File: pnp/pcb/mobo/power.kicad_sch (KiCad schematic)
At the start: 30 parts, among them J31 Barrel_Jack_Switch, J34 Screw_Terminal_01x02, U11 FDS4435BZ, U12 TPS54331, U13 AP1117-33

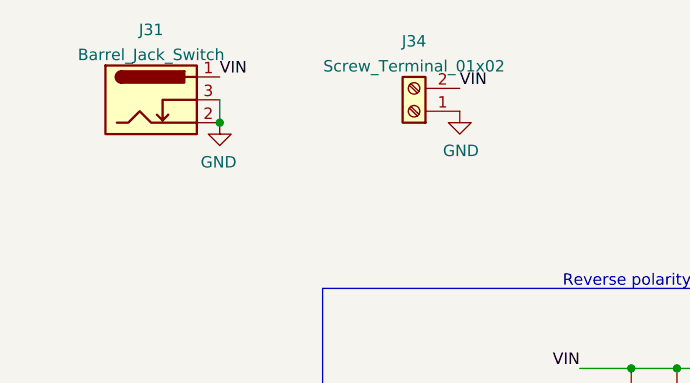
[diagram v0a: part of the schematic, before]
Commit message: adds custom combo power jack footprint for both barrel jack and terminal block
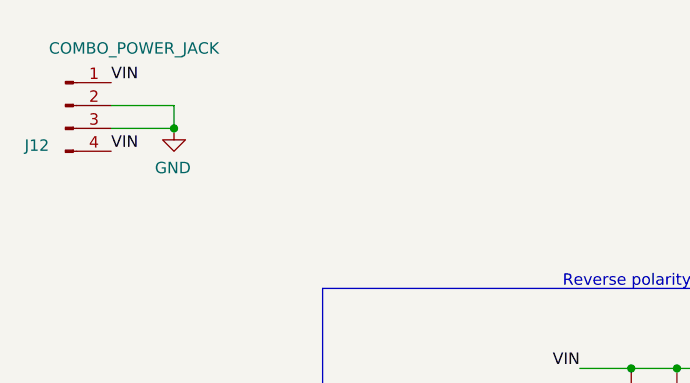
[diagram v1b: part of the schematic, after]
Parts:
- removed J31: Barrel_Jack_Switch, Connector_BarrelJack:BarrelJack_Horizontal, symbol Connector:Barrel_Jack_Switch
- removed J34: Screw_Terminal_01x02, TerminalBlock_RND:TerminalBlock_RND_205-00001_1x02_P5.00mm_Horizontal, symbol Connector:Screw_Terminal_01x02
- added J12: COMBO_POWER_JACK, index:BarrelJack_Horizontal, symbol Connector:Conn_01x04_Male
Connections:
- net GND: now also J12.2 (Pin_2), J12.3 (Pin_3)
- net VIN: now also J12.1 (Pin_1), J12.4 (Pin_4)
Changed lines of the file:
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@@
   (junction (at 121.92 55.88) (diameter 0) (color 0 0 0 0)
   )
+  (junction (at 45.72 29.21) (diameter 0) (color 0 0 0 0)
+  )
   (junction (at 121.92 64.77) (diameter 0) (color 0 0 0 0)
   )
@@
   )
   (junction (at 118.11 104.14) (diameter 0) (color 0 0 0 0)
-  )
-  (junction (at 50.8 28.575) (diameter 0) (color 0 0 0 0)
   )
   (junction (at 158.75 140.97) (diameter 0) (color 0 0 0 0)
@@
     (stroke (width 0) (type default) (color 0 0 0 0))
   )
+  (wire (pts (xy 38.735 29.21) (xy 45.72 29.21))
+    (stroke (width 0) (type default) (color 0 0 0 0))
+  )
   (polyline (pts (xy 167.64 157.48) (xy 134.62 157.48))
     (stroke (width 0) (type default) (color 0 0 0 0))
@@
     (stroke (width 0) (type default) (color 0 0 0 0))
   )
+  (wire (pts (xy 38.735 26.67) (xy 45.72 26.67))
+    (stroke (width 0) (type default) (color 0 0 0 0))
+  )
   (wire (pts (xy 182.88 100.33) (xy 182.88 101.6))
     (stroke (width 0) (type default) (color 0 0 0 0))
@@
     (stroke (width 0) (type default) (color 0 0 0 0))
   )
+  (wire (pts (xy 45.72 26.67) (xy 45.72 29.21))
+    (stroke (width 0) (type default) (color 0 0 0 0))
+  )
   (wire (pts (xy 121.92 64.77) (xy 123.19 64.77))
     (stroke (width 0) (type default) (color 0 0 0 0))
@@
   )
   (wire (pts (xy 92.71 152.4) (xy 97.79 152.4))
-    (stroke (width 0) (type default) (color 0 0 0 0))
-  )
-  (wire (pts (xy 50.8 26.035) (xy 50.8 28.575))
     (stroke (width 0) (type default) (color 0 0 0 0))
   )
@@
     (effects (font (size 1.27 1.27)) (justify right bottom))
   )
-  (label "VIN" (at 77.47 24.765 0)
+  (label "VIN" (at 38.735 31.75 0)
     (effects (font (size 1.27 1.27)) (justify left bottom))
   )
-  (label "VIN" (at 50.8 23.495 0)
+  (label "VIN" (at 38.735 24.13 0)
     (effects (font (size 1.27 1.27)) (justify left bottom))
   )
@@
     (pin "1")
   )
-  (symbol (lib_id "Connector:Screw_Terminal_01x02") (at 72.39 27.305 180) (unit 1)
-    (in_bom yes) (on_board yes) (fields_autoplaced)
-    (property "Reference" "J34" (id 0) (at 72.39 19.5285 0))
-    (property "Value" "Screw_Terminal_01x02" (id 1) (at 72.39 22.3036 0))
-    (property "Footprint" "TerminalBlock_RND:TerminalBlock_RND_205-00001_1x02_P5.00mm_Horizontal" (id 2) (at 72.39 27.305 0)
-      (effects (font (size 1.27 1.27)) hide)
-    )
-    (property "Datasheet" "~" (id 3) (at 72.39 27.305 0)
-      (effects (font (size 1.27 1.27)) hide)
-    )
-    (pin "1")
-    (pin "2")
-  )
   (symbol (lib_id "power:PWR_FLAG") (at 123.19 64.77 270) (unit 1)
     (in_bom yes) (on_board yes)
@@
     (pin "1")
   )
-  (symbol (lib_id "power:GND") (at 50.8 28.575 0) (mirror y) (unit 1)
-    (in_bom yes) (on_board yes)
-    (property "Reference" "#PWR0247" (id 0) (at 50.8 34.925 0)
-      (effects (font (size 1.27 1.27)) hide)
-    )
-    (property "Value" "GND" (id 1) (at 50.673 32.9692 0))
-    (property "Footprint" "" (id 2) (at 50.8 28.575 0)
-      (effects (font (size 1.27 1.27)) hide)
-    )
-    (property "Datasheet" "" (id 3) (at 50.8 28.575 0)
-      (effects (font (size 1.27 1.27)) hide)
-    )
-    (pin "1")
-  )
   (symbol (lib_id "Device:D_Schottky_Small") (at 100.33 152.4 180) (unit 1)
     (in_bom yes) (on_board yes)
@@
     (pin "2")
   )
-  (symbol (lib_id "power:GND") (at 77.47 27.305 0) (unit 1)
-    (in_bom yes) (on_board yes)
-    (property "Reference" "#PWR0251" (id 0) (at 77.47 33.655 0)
-      (effects (font (size 1.27 1.27)) hide)
-    )
-    (property "Value" "GND" (id 1) (at 77.597 31.6992 0))
-    (property "Footprint" "" (id 2) (at 77.47 27.305 0)
-      (effects (font (size 1.27 1.27)) hide)
-    )
-    (property "Datasheet" "" (id 3) (at 77.47 27.305 0)
+  (symbol (lib_id "power:GND") (at 45.72 29.21 0) (mirror y) (unit 1)
+    (in_bom yes) (on_board yes)
+    (property "Reference" "#PWR0246" (id 0) (at 45.72 35.56 0)
+      (effects (font (size 1.27 1.27)) hide)
+    )
+    (property "Value" "GND" (id 1) (at 45.593 33.6042 0))
+    (property "Footprint" "" (id 2) (at 45.72 29.21 0)
+      (effects (font (size 1.27 1.27)) hide)
+    )
+    (property "Datasheet" "" (id 3) (at 45.72 29.21 0)
       (effects (font (size 1.27 1.27)) hide)
     )
@@
     (pin "1")
   )
-  (symbol (lib_id "Connector:Barrel_Jack_Switch") (at 43.18 26.035 0) (unit 1)
-    (in_bom yes) (on_board yes) (fields_autoplaced)
-    (property "Reference" "J31" (id 0) (at 43.18 18.2585 0))
-    (property "Value" "Barrel_Jack_Switch" (id 1) (at 43.18 21.0336 0))
-    (property "Footprint" "Connector_BarrelJack:BarrelJack_Horizontal" (id 2) (at 44.45 27.051 0)
-      (effects (font (size 1.27 1.27)) hide)
-    )
-    (property "Datasheet" "~" (id 3) (at 44.45 27.051 0)
+  (symbol (lib_id "Device:D_Schottky_Small") (at 100.33 160.02 180) (unit 1)
+    (in_bom yes) (on_board yes)
+    (property "Reference" "D4" (id 0) (at 101.4984 162.052 90)
+      (effects (font (size 1.27 1.27)) (justify left))
+    )
+    (property "Value" "SS34" (id 1) (at 99.06 163.83 0)
+      (effects (font (size 1.27 1.27)) (justify left))
+    )
+    (property "Footprint" "Diode_SMD:D_SMA" (id 2) (at 100.33 160.02 0)
+      (effects (font (size 1.27 1.27)) hide)
+    )
+    (property "Datasheet" "~" (id 3) (at 100.33 160.02 0)
+      (effects (font (size 1.27 1.27)) hide)
+    )
+    (property "LCSC" "C266553" (id 4) (at 100.33 160.02 90)
+      (effects (font (size 1.27 1.27)) hide)
+    )
+    (property "JLCPCB" "C8678" (id 5) (at 100.33 160.02 90)
+      (effects (font (size 1.27 1.27)) hide)
+    )
+    (property "Notes" "Vf<=0.55V,I>=2A,Vr>=24V" (id 6) (at 100.33 160.02 90)
+      (effects (font (size 1.27 1.27)) hide)
+    )
+    (property "Config" "" (id 7) (at 100.33 160.02 0)
+      (effects (font (size 1.27 1.27)) hide)
+    )
+    (property "Digikey" "641-2115-1-ND" (id 8) (at 100.33 160.02 0)
+      (effects (font (size 1.27 1.27)) hide)
+    )
+    (property "Mouser" "821-SS34LRVG" (id 9) (at 100.33 160.02 0)
+      (effects (font (size 1.27 1.27)) hide)
+    )
+    (pin "1")
+    (pin "2")
+  )
+  (symbol (lib_id "Device:C_Small") (at 101.6 58.42 180) (unit 1)
+    (in_bom yes) (on_board yes)
+    (property "Reference" "C38" (id 0) (at 104.14 58.42 0)
+      (effects (font (size 1.27 1.27)) (justify right))
+    )
+    (property "Value" "22u" (id 1) (at 104.14 60.96 0)
+      (effects (font (size 1.27 1.27)) (justify right))
+    )
+    (property "Footprint" "Capacitor_SMD:C_0805_2012Metric" (id 2) (at 100.6348 54.61 0)
+      (effects (font (size 1.27 1.27)) hide)
+    )
+    (property "Datasheet" "" (id 3) (at 101.6 58.42 0)
+      (effects (font (size 1.27 1.27)) hide)
+    )
+    (property "Digikey" "" (id 4) (at 101.6 58.42 0)
+      (effects (font (size 1.27 1.27)) hide)
+    )
+    (property "JLCPCB" "C45783" (id 5) (at 101.6 58.42 0)
+      (effects (font (size 1.27 1.27)) hide)
+    )
+    (property "LCSC" "C5674" (id 6) (at 101.6 58.42 0)
+      (effects (font (size 1.27 1.27)) hide)
+    )
+    (property "Mouser" "" (id 7) (at 101.6 58.42 0)
+      (effects (font (size 1.27 1.27)) hide)
+    )
+    (pin "1")
+    (pin "2")
+  )
+  (symbol (lib_id "Connector:Conn_01x04_Male") (at 33.655 26.67 0) (unit 1)
+    (in_bom yes) (on_board yes)
+    (property "Reference" "J12" (id 0) (at 30.48 31.115 0))
+    (property "Value" "COMBO_POWER_JACK" (id 1) (at 41.275 20.32 0))
+    (property "Footprint" "index:BarrelJack_Horizontal" (id 2) (at 33.655 26.67 0)
+      (effects (font (size 1.27 1.27)) hide)
+    )
+    (property "Datasheet" "~" (id 3) (at 33.655 26.67 0)
       (effects (font (size 1.27 1.27)) hide)
     )
@@
     (pin "2")
     (pin "3")
-  )
-  (symbol (lib_id "Device:D_Schottky_Small") (at 100.33 160.02 180) (unit 1)
-    (in_bom yes) (on_board yes)
-    (property "Reference" "D4" (id 0) (at 101.4984 162.052 90)
-      (effects (font (size 1.27 1.27)) (justify left))
-    )
-    (property "Value" "SS34" (id 1) (at 99.06 163.83 0)
-      (effects (font (size 1.27 1.27)) (justify left))
-    )
-    (property "Footprint" "Diode_SMD:D_SMA" (id 2) (at 100.33 160.02 0)
-      (effects (font (size 1.27 1.27)) hide)
-    )
-    (property "Datasheet" "~" (id 3) (at 100.33 160.02 0)
-      (effects (font (size 1.27 1.27)) hide)
-    )
-    (property "LCSC" "C266553" (id 4) (at 100.33 160.02 90)
-      (effects (font (size 1.27 1.27)) hide)
-    )
-    (property "JLCPCB" "C8678" (id 5) (at 100.33 160.02 90)
-      (effects (font (size 1.27 1.27)) hide)
-    )
-    (property "Notes" "Vf<=0.55V,I>=2A,Vr>=24V" (id 6) (at 100.33 160.02 90)
-      (effects (font (size 1.27 1.27)) hide)
-    )
-    (property "Config" "" (id 7) (at 100.33 160.02 0)
-      (effects (font (size 1.27 1.27)) hide)
-    )
-    (property "Digikey" "641-2115-1-ND" (id 8) (at 100.33 160.02 0)
-      (effects (font (size 1.27 1.27)) hide)
-    )
-    (property "Mouser" "821-SS34LRVG" (id 9) (at 100.33 160.02 0)
-      (effects (font (size 1.27 1.27)) hide)
-    )
-    (pin "1")
-    (pin "2")
-  )
-  (symbol (lib_id "Device:C_Small") (at 101.6 58.42 180) (unit 1)
-    (in_bom yes) (on_board yes)
-    (property "Reference" "C38" (id 0) (at 104.14 58.42 0)
-      (effects (font (size 1.27 1.27)) (justify right))
-    )
-    (property "Value" "22u" (id 1) (at 104.14 60.96 0)
-      (effects (font (size 1.27 1.27)) (justify right))
-    )
-    (property "Footprint" "Capacitor_SMD:C_0805_2012Metric" (id 2) (at 100.6348 54.61 0)
-      (effects (font (size 1.27 1.27)) hide)
-    )
-    (property "Datasheet" "" (id 3) (at 101.6 58.42 0)
-      (effects (font (size 1.27 1.27)) hide)
-    )
-    (property "Digikey" "" (id 4) (at 101.6 58.42 0)
-      (effects (font (size 1.27 1.27)) hide)
-    )
-    (property "JLCPCB" "C45783" (id 5) (at 101.6 58.42 0)
-      (effects (font (size 1.27 1.27)) hide)
-    )
-    (property "LCSC" "C5674" (id 6) (at 101.6 58.42 0)
-      (effects (font (size 1.27 1.27)) hide)
-    )
-    (property "Mouser" "" (id 7) (at 101.6 58.42 0)
-      (effects (font (size 1.27 1.27)) hide)
-    )
-    (pin "1")
-    (pin "2")
+    (pin "4")
   )
 )

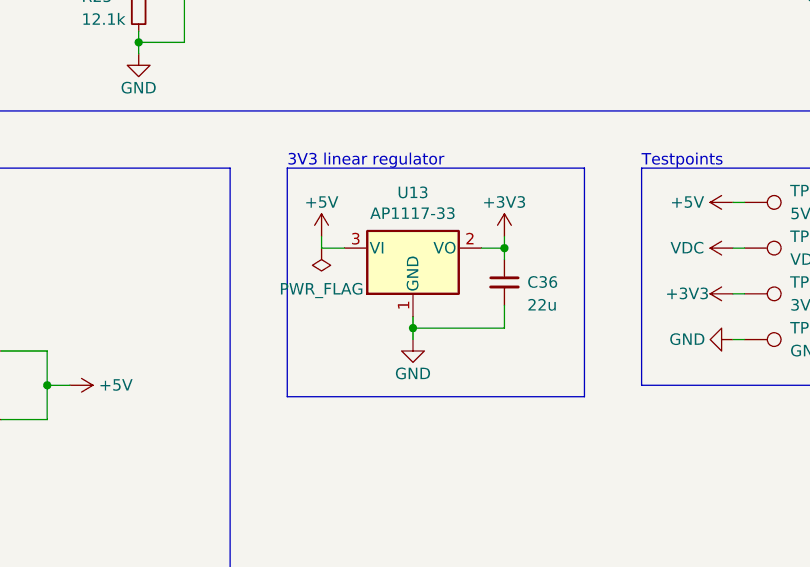
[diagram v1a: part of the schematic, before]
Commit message: edits some USB stuff. trying a system where the hub is not present, and the board acts as a passthrough and power supply for the bottom camera, and the top is connected directly.
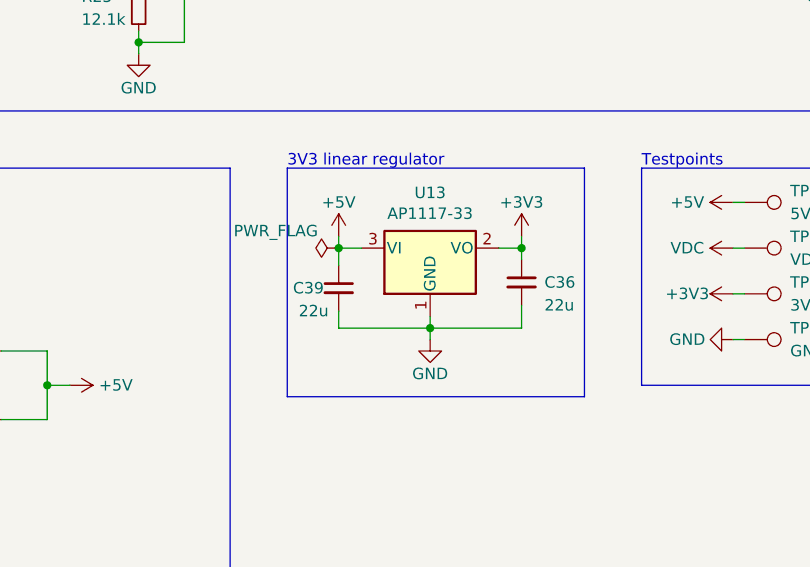
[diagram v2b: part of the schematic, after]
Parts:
- added C39: 22u, Capacitor_SMD:C_0805_2012Metric, symbol Device:C_Small
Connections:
- net +5V: now also C39.1
- net GND: now also C39.2
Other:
- moved on the sheet: C36, U13

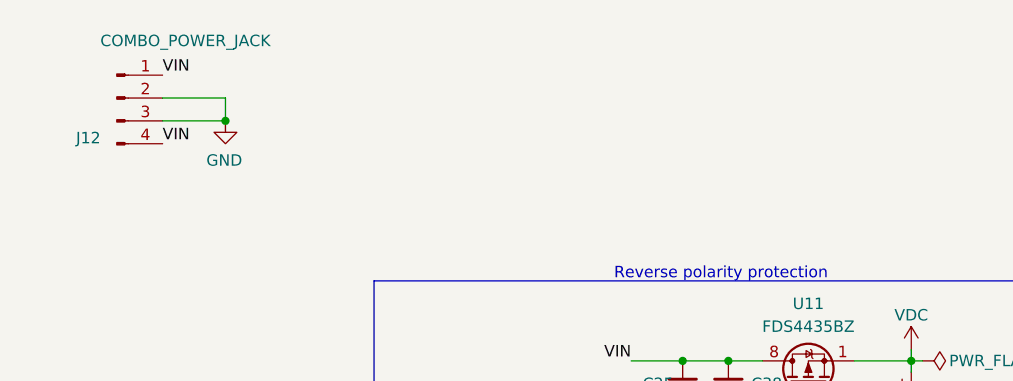
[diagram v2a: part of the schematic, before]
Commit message: adds fuse, esd protection to USB lines, removes usb hub, switches to chonky usb type b
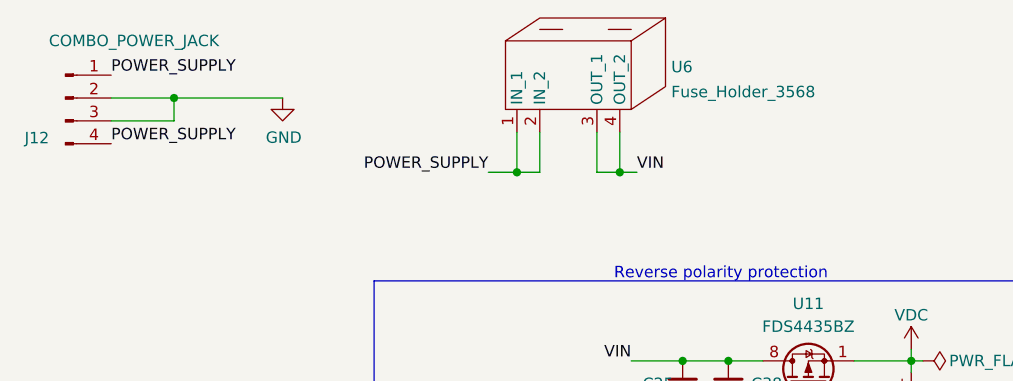
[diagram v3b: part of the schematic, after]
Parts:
- added U6: Fuse_Holder_3568, index:Fuse_Holder_3568, symbol index:Fuse_Holder_3568
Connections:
- net VIN: now also U6.3 (OUT_1), U6.4 (OUT_2); no longer J12.1 (Pin_1), J12.4 (Pin_4)
- new net POWER_SUPPLY: J12.1 (Pin_1), J12.4 (Pin_4), U6.1 (IN_1), U6.2 (IN_2)
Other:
- moved on the sheet: J12
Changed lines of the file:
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@@
   (junction (at 121.92 55.88) (diameter 0) (color 0 0 0 0)
   )
-  (junction (at 45.72 29.21) (diameter 0) (color 0 0 0 0)
-  )
   (junction (at 121.92 64.77) (diameter 0) (color 0 0 0 0)
   )
@@
   (junction (at 118.11 104.14) (diameter 0) (color 0 0 0 0)
   )
+  (junction (at 40.005 26.67) (diameter 0) (color 0 0 0 0)
+  )
   (junction (at 140.335 140.97) (diameter 0) (color 0 0 0 0)
   )
+  (junction (at 89.535 34.925) (diameter 0) (color 0 0 0 0)
+  )
   (junction (at 160.655 140.97) (diameter 0) (color 0 0 0 0)
   )
@@
   )
   (junction (at 101.6 64.77) (diameter 0) (color 0 0 0 0)
+  )
+  (junction (at 78.105 34.925) (diameter 0) (color 0 0 0 0)
   )
   (junction (at 101.6 55.88) (diameter 0) (color 0 0 0 0)
@@
     (stroke (width 0) (type default) (color 0 0 0 0))
   )
-  (wire (pts (xy 38.735 29.21) (xy 45.72 29.21))
+  (wire (pts (xy 33.02 29.21) (xy 40.005 29.21))
+    (stroke (width 0) (type default) (color 0 0 0 0))
+  )
+  (wire (pts (xy 40.005 26.67) (xy 52.07 26.67))
     (stroke (width 0) (type default) (color 0 0 0 0))
   )
@@
     (stroke (width 0) (type default) (color 0 0 0 0))
   )
-  (wire (pts (xy 38.735 26.67) (xy 45.72 26.67))
+  (wire (pts (xy 89.535 30.48) (xy 89.535 34.925))
+    (stroke (width 0) (type default) (color 0 0 0 0))
+  )
+  (wire (pts (xy 33.02 26.67) (xy 40.005 26.67))
     (stroke (width 0) (type default) (color 0 0 0 0))
   )
@@
     (stroke (width 0) (type default) (color 0 0 0 0))
   )
+  (wire (pts (xy 78.105 34.925) (xy 80.645 34.925))
+    (stroke (width 0) (type default) (color 0 0 0 0))
+  )
   (wire (pts (xy 118.11 104.14) (xy 118.11 99.06))
     (stroke (width 0) (type default) (color 0 0 0 0))
@@
     (stroke (width 0) (type default) (color 0 0 0 0))
   )
-  (wire (pts (xy 45.72 26.67) (xy 45.72 29.21))
+  (wire (pts (xy 40.005 26.67) (xy 40.005 29.21))
+    (stroke (width 0) (type default) (color 0 0 0 0))
+  )
+  (wire (pts (xy 86.995 34.925) (xy 89.535 34.925))
     (stroke (width 0) (type default) (color 0 0 0 0))
   )
@@
     (stroke (width 0) (type default) (color 0 0 0 0))
   )
+  (wire (pts (xy 89.535 34.925) (xy 91.44 34.925))
+    (stroke (width 0) (type default) (color 0 0 0 0))
+  )
   (wire (pts (xy 118.11 118.11) (xy 118.11 119.38))
     (stroke (width 0) (type default) (color 0 0 0 0))
@@
     (stroke (width 0) (type default) (color 0 0 0 0))
   )
+  (wire (pts (xy 78.105 30.48) (xy 78.105 34.925))
+    (stroke (width 0) (type default) (color 0 0 0 0))
+  )
+  (wire (pts (xy 74.93 34.925) (xy 78.105 34.925))
+    (stroke (width 0) (type default) (color 0 0 0 0))
+  )
   (wire (pts (xy 106.68 96.52) (xy 106.68 97.79))
     (stroke (width 0) (type default) (color 0 0 0 0))
@@
     (stroke (width 0) (type default) (color 0 0 0 0))
   )
+  (wire (pts (xy 86.995 30.48) (xy 86.995 34.925))
+    (stroke (width 0) (type default) (color 0 0 0 0))
+  )
   (polyline (pts (xy 128.27 132.08) (xy 128.27 177.8))
     (stroke (width 0) (type default) (color 0 0 0 0))
   )
   (wire (pts (xy 96.52 88.9) (xy 121.92 88.9))
+    (stroke (width 0) (type default) (color 0 0 0 0))
+  )
+  (wire (pts (xy 80.645 34.925) (xy 80.645 30.48))
     (stroke (width 0) (type default) (color 0 0 0 0))
   )
@@
     (effects (font (size 1.27 1.27)) (justify right bottom))
   )
-  (label "VIN" (at 38.735 31.75 0)
+  (label "POWER_SUPPLY" (at 74.93 34.925 180)
+    (effects (font (size 1.27 1.27)) (justify right bottom))
+  )
+  (label "POWER_SUPPLY" (at 33.02 31.75 0)
     (effects (font (size 1.27 1.27)) (justify left bottom))
   )
-  (label "VIN" (at 38.735 24.13 0)
+  (label "VIN" (at 91.44 34.925 0)
+    (effects (font (size 1.27 1.27)) (justify left bottom))
+  )
+  (label "POWER_SUPPLY" (at 33.02 24.13 0)
     (effects (font (size 1.27 1.27)) (justify left bottom))
   )
@@
     (pin "2")
   )
-  (symbol (lib_id "power:GND") (at 45.72 29.21 0) (mirror y) (unit 1)
-    (in_bom yes) (on_board yes)
-    (property "Reference" "#PWR0246" (id 0) (at 45.72 35.56 0)
-      (effects (font (size 1.27 1.27)) hide)
-    )
-    (property "Value" "GND" (id 1) (at 45.593 33.6042 0))
-    (property "Footprint" "" (id 2) (at 45.72 29.21 0)
-      (effects (font (size 1.27 1.27)) hide)
-    )
-    (property "Datasheet" "" (id 3) (at 45.72 29.21 0)
-      (effects (font (size 1.27 1.27)) hide)
-    )
-    (pin "1")
+  (symbol (lib_id "power:GND") (at 52.07 26.67 0) (unit 1)
+    (in_bom yes) (on_board yes)
+    (property "Reference" "#PWR0246" (id 0) (at 52.07 33.02 0)
+      (effects (font (size 1.27 1.27)) hide)
+    )
+    (property "Value" "GND" (id 1) (at 52.197 31.0642 0))
+    (property "Footprint" "" (id 2) (at 52.07 26.67 0)
+      (effects (font (size 1.27 1.27)) hide)
+    )
+    (property "Datasheet" "" (id 3) (at 52.07 26.67 0)
+      (effects (font (size 1.27 1.27)) hide)
+    )
+    (pin "1")
+  )
+  (symbol (lib_id "index:Fuse_Holder_3568") (at 86.995 38.1 0) (unit 1)
+    (in_bom yes) (on_board yes) (fields_autoplaced)
+    (property "Reference" "U6" (id 0) (at 95.25 23.2215 0)
+      (effects (font (size 1.27 1.27)) (justify left))
+    )
+    (property "Value" "Fuse_Holder_3568" (id 1) (at 95.25 25.9966 0)
+      (effects (font (size 1.27 1.27)) (justify left))
+    )
+    (property "Footprint" "index:Fuse_Holder_3568" (id 2) (at 86.995 38.1 0)
+      (effects (font (size 1.27 1.27)) hide)
+    )
+    (property "Datasheet" "" (id 3) (at 86.995 38.1 0)
+      (effects (font (size 1.27 1.27)) hide)
+    )
+    (pin "1")
+    (pin "2")
+    (pin "3")
+    (pin "4")
   )
   (symbol (lib_id "power:+5VP") (at 194.31 92.71 0) (unit 1)
@@
     (pin "2")
   )
-  (symbol (lib_id "Connector:Conn_01x04_Male") (at 33.655 26.67 0) (unit 1)
-    (in_bom yes) (on_board yes)
-    (property "Reference" "J12" (id 0) (at 30.48 31.115 0))
-    (property "Value" "COMBO_POWER_JACK" (id 1) (at 41.275 20.32 0))
-    (property "Footprint" "index:BarrelJack_Horizontal" (id 2) (at 33.655 26.67 0)
-      (effects (font (size 1.27 1.27)) hide)
-    )
-    (property "Datasheet" "~" (id 3) (at 33.655 26.67 0)
-      (effects (font (size 1.27 1.27)) hide)
-    )
+  (symbol (lib_id "Connector:Conn_01x04_Male") (at 27.94 26.67 0) (unit 1)
+    (in_bom yes) (on_board yes)
+    (property "Reference" "J12" (id 0) (at 24.765 31.115 0))
+    (property "Value" "COMBO_POWER_JACK" (id 1) (at 35.56 20.32 0))
+    (property "Footprint" "index:BarrelJack_Horizontal" (id 2) (at 27.94 26.67 0)
+      (effects (font (size 1.27 1.27)) hide)
+    )
+    (property "Datasheet" "~" (id 3) (at 27.94 26.67 0)
+      (effects (font (size 1.27 1.27)) hide)
+    )
